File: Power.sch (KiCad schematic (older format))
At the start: 11 parts, among them P1 CONN_12X2, SW1 SWITCH_INV

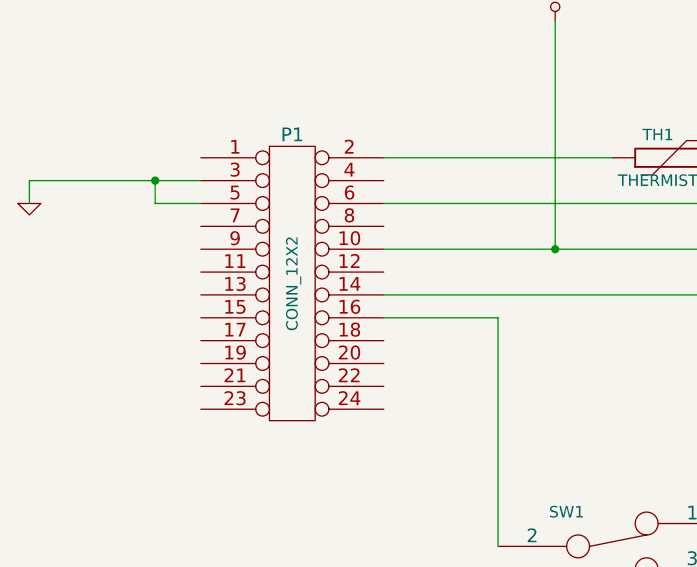
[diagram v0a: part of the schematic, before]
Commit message: 5.6 Video 1/2 Associating and Placing the Terminal/ATX Blocks
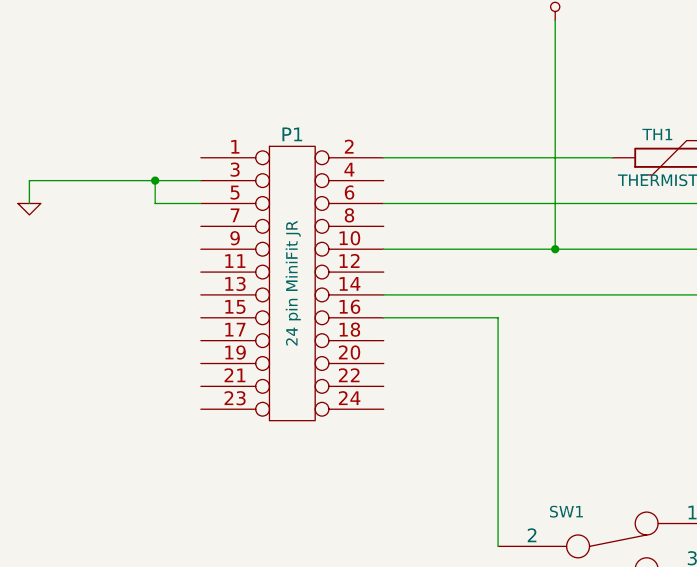
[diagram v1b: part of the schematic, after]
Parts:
- P1: value CONN_12X2 -> 24 pin MiniFit JR; MFG Name (none) -> molex; MFG Part Number (none) -> 39-30-1240
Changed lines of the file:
@@
 LIBS:BenchBudEE
 LIBS:BenchBudEE-cache
-EELAYER 24 0
+EELAYER 27 0
 EELAYER END
 $Descr A4 11693 8268
@@
 Sheet 3 9
 Title ""
-Date "21 feb 2014"
+Date "22 feb 2014"
 Rev ""
 Comp ""
@@
 P 2150 2650
 F 0 "P1" H 2150 3300 60  0000 C CNN
-F 1 "CONN_12X2" V 2150 2650 50  0000 C CNN
+F 1 "24 pin MiniFit JR" V 2150 2650 50  0000 C CNN
 F 2 "" H 2150 2650 60  0000 C CNN
 F 3 "" H 2150 2650 60  0000 C CNN
+F 4 "molex" H 2150 2650 60  0001 C CNN "MFG Name"
+F 5 "39-30-1240" H 2150 2650 60  0001 C CNN "MFG Part Number"
 	1    2150 2650
 	1    0    0    -1

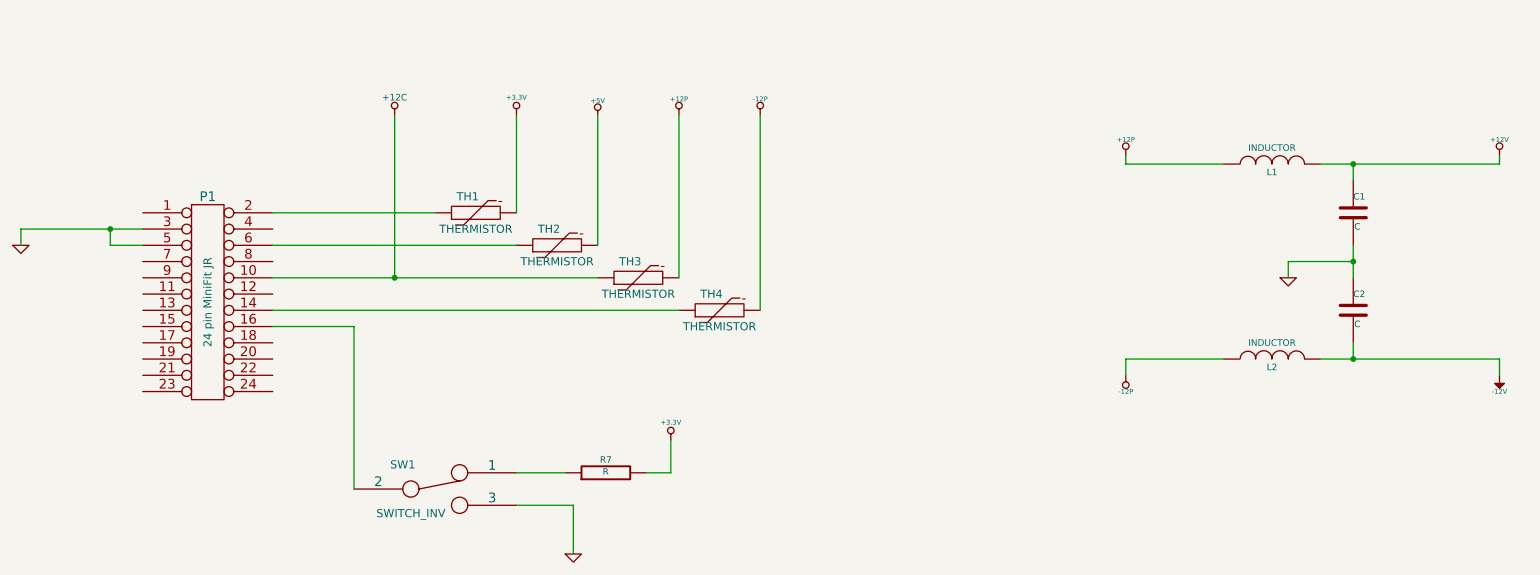
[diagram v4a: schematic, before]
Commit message: 5.8 Associating and Placing the Power Protection and Filtering Module
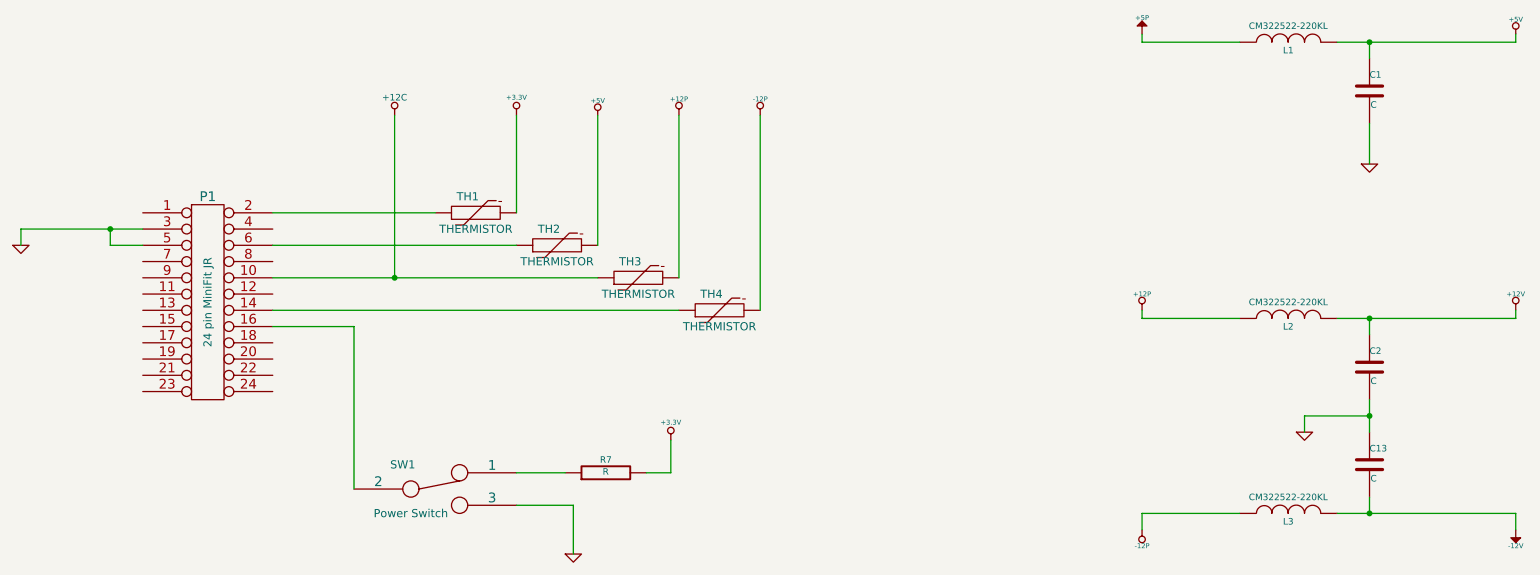
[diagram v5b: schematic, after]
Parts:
- added C13: C, ~, symbol C
- added L3: CM322522-220KL, ~, symbol INDUCTOR
- L1, L2: value INDUCTOR -> CM322522-220KL; MFG Name (none) -> Bournes; MFG Part Number (none) -> CM322522-220KL
- SW1: value SWITCH_INV -> Power Switch; MFG Name (none) -> C&K Components; MFG Part Number (none) -> OS102011MA1QN1
- TH1, TH2, TH3, TH4: MFG Name (none) -> TE Connectivity; MFG Part Number (none) -> MINISMDC050F-2
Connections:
- net +12P: now also L2.1; no longer L1.1
- net +12V: now also C2.1, L2.2; no longer C1.1, L1.2
- net +5V: now also C1.1, L1.2
- net -12P: now also L3.1; no longer L2.1
- net -12V: now also C13.2, L3.2; no longer C2.2, L2.2
- net GND: now also C2.2, C13.1; no longer C2.1
- new net +5P: L1.1
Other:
- moved on the sheet: C1, L1

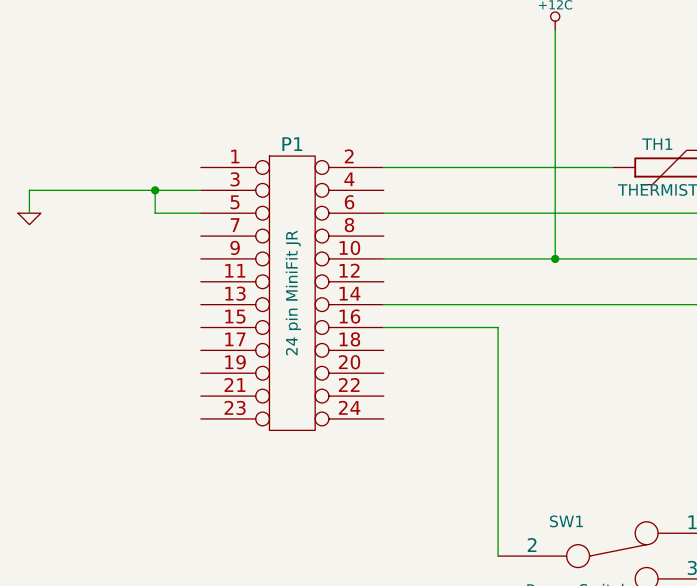
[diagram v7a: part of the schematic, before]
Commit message: Cleanup/ERC checks, etc (on my own, no video)
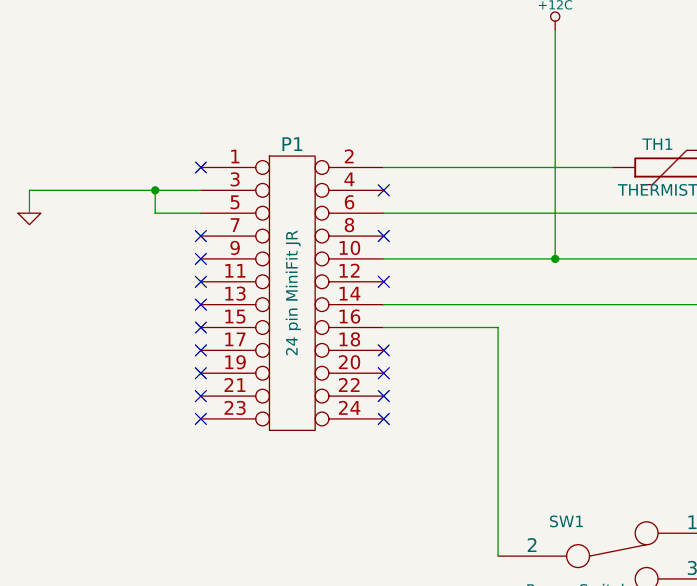
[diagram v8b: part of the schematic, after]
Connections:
- no-connect marks 0 -> 17
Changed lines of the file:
@@
 Wire Wire Line
 	9300 1550 9300 1800
+NoConn ~ 2550 2200
+NoConn ~ 2550 2400
+NoConn ~ 2550 2600
+NoConn ~ 2550 2900
+NoConn ~ 2550 3000
+NoConn ~ 2550 3100
+NoConn ~ 2550 3200
+NoConn ~ 1750 3200
+NoConn ~ 1750 3100
+NoConn ~ 1750 3000
+NoConn ~ 1750 2900
+NoConn ~ 1750 2800
+NoConn ~ 1750 2700
+NoConn ~ 1750 2600
+NoConn ~ 1750 2500
+NoConn ~ 1750 2400
+NoConn ~ 1750 2100
 $EndSCHEMATC
